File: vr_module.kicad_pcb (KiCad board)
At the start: 4 copper layers, 16.9 x 22.6 mm, 32 parts, among them J1 Conn_01x07, U1 LM393, U2 NC7SB3157P6X, U3 74HC00, U4 NC7SB3157P6X, U5 SRV05-4, U6 MCP6004

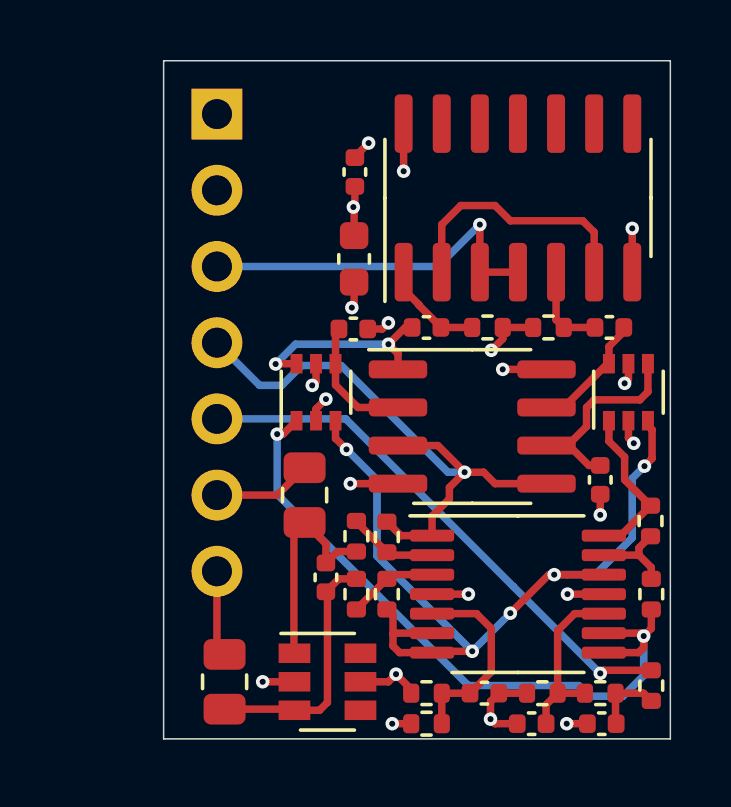
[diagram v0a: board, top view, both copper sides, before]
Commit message: ground unused inputs to NAND
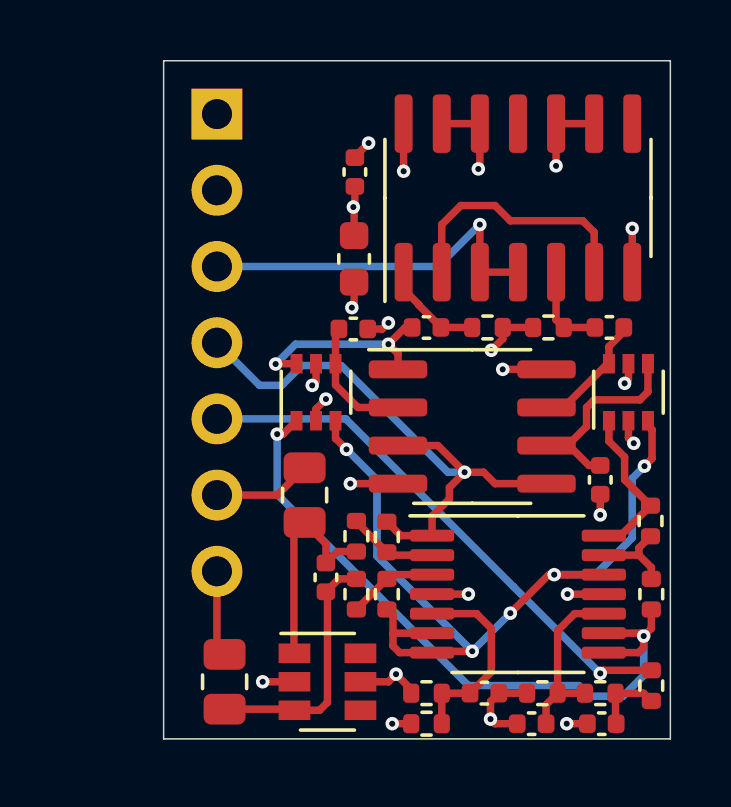
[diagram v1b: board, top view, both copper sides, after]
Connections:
- U3 pad 10: (no net) -> GND
- U3 pad 12: (no net) -> GND
- U3 pad 13: (no net) -> GND
- U3 pad 9: (no net) -> GND
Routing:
- net GND: track 16.1 -> 21.6 mm, vias 14 -> 16

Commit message: upgrade comparator
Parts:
- U1: value LM393 -> MAX9142

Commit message: I heard we like LEDs
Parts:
- added D1: LED, LED_SMD:LED_0603_1608Metric, F.Cu at (62.6, 84.8)
- added R16: 2.2k, Resistor_SMD:R_0402_1005Metric, F.Cu at (62.6, 82.2)
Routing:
- net output: track 12.2 -> 14.9 mm
- net Net-(D1-Pad1): track 0.00 -> 1.30 mm
- net GND: track 21.6 -> 22.3 mm, vias 16 -> 17
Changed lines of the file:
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@@
     (thickness 1.6)
     (drawings 11)
-    (tracks 254)
+    (tracks 261)
     (zones 0)
-    (modules 32)
-    (nets 26)
+    (modules 34)
+    (nets 27)
   )
   (page A4)
@@
   (net 24 "Net-(C9-Pad2)")
   (net 25 "Net-(C10-Pad2)")
+  (net 26 "Net-(D1-Pad1)")
   (net_class Default "This is the default net class."
     (clearance 0.1524)
@@
     (add_net "Net-(C8-Pad1)")
     (add_net "Net-(C9-Pad2)")
+    (add_net "Net-(D1-Pad1)")
     (add_net "Net-(R13-Pad1)")
     (add_net "Net-(R3-Pad1)")
@@
     (add_net thresh_input)
     (add_net thresh_low)
+  )
+  (module Resistor_SMD:R_0402_1005Metric (layer F.Cu)
+    (at 62.5904 82.2452 270)
+    (descr "Resistor SMD 0402 (1005 Metric), square (rectangular) end terminal, IPC_7351 nominal, (Body size source: IPC-SM-782 page 72, https://www.pcb-3d.com/wordpress/wp-content/uploads/ipc-sm-782a_amendment_1_and_2.pdf), generated with kicad-footprint-generator")
+    (tags resistor)
+    (attr smd)
+    (fp_text reference R16 (at 0 -1.17 90) (layer F.SilkS) hide
+      (effects (font (size 1 1) (thickness 0.15)))
+    )
+    (fp_text value 2.2k (at 0 1.17 90) (layer F.Fab)
+      (effects (font (size 1 1) (thickness 0.15)))
+    )
+    (fp_text user %R (at 0 0 90) (layer F.Fab)
+      (effects (font (size 0.26 0.26) (thickness 0.04)))
+    )
+    (fp_line (start -0.525 0.27) (end -0.525 -0.27) (layer F.Fab) (width 0.1))
+    (fp_line (start -0.525 -0.27) (end 0.525 -0.27) (layer F.Fab) (width 0.1))
+    (fp_line (start 0.525 -0.27) (end 0.525 0.27) (layer F.Fab) (width 0.1))
+    (fp_line (start 0.525 0.27) (end -0.525 0.27) (layer F.Fab) (width 0.1))
+    (fp_line (start -0.153641 -0.38) (end 0.153641 -0.38) (layer F.SilkS) (width 0.12))
+    (fp_line (start -0.153641 0.38) (end 0.153641 0.38) (layer F.SilkS) (width 0.12))
+    (fp_line (start -0.93 0.47) (end -0.93 -0.47) (layer F.CrtYd) (width 0.05))
+    (fp_line (start -0.93 -0.47) (end 0.93 -0.47) (layer F.CrtYd) (width 0.05))
+    (fp_line (start 0.93 -0.47) (end 0.93 0.47) (layer F.CrtYd) (width 0.05))
+    (fp_line (start 0.93 0.47) (end -0.93 0.47) (layer F.CrtYd) (width 0.05))
+    (pad 2 smd roundrect (at 0.51 0 270) (size 0.54 0.64) (layers F.Cu F.Paste F.Mask) (roundrect_rratio 0.25)
+      (net 26 "Net-(D1-Pad1)"))
+    (pad 1 smd roundrect (at -0.51 0 270) (size 0.54 0.64) (layers F.Cu F.Paste F.Mask) (roundrect_rratio 0.25)
+      (net 5 GND))
+    (model ${KISYS3DMOD}/Resistor_SMD.3dshapes/R_0402_1005Metric.wrl
+      (at (xyz 0 0 0))
+      (scale (xyz 1 1 1))
+      (rotate (xyz 0 0 0))
+    )
+  )
+  (module LED_SMD:LED_0603_1608Metric (layer F.Cu)
+    (at 62.5856 84.836 270)
+    (descr "LED SMD 0603 (1608 Metric), square (rectangular) end terminal, IPC_7351 nominal, (Body size source: http://www.tortai-tech.com/upload/download/2011102023233369053.pdf), generated with kicad-footprint-generator")
+    (tags LED)
+    (attr smd)
+    (fp_text reference D1 (at 0 -1.43 90) (layer F.SilkS) hide
+      (effects (font (size 1 1) (thickness 0.15)))
+    )
+    (fp_text value LED (at 0 1.43 90) (layer F.Fab)
+      (effects (font (size 1 1) (thickness 0.15)))
+    )
+    (fp_text user %R (at 0 0 90) (layer F.Fab)
+      (effects (font (size 0.4 0.4) (thickness 0.06)))
+    )
+    (fp_line (start 0.8 -0.4) (end -0.5 -0.4) (layer F.Fab) (width 0.1))
+    (fp_line (start -0.5 -0.4) (end -0.8 -0.1) (layer F.Fab) (width 0.1))
+    (fp_line (start -0.8 -0.1) (end -0.8 0.4) (layer F.Fab) (width 0.1))
+    (fp_line (start -0.8 0.4) (end 0.8 0.4) (layer F.Fab) (width 0.1))
+    (fp_line (start 0.8 0.4) (end 0.8 -0.4) (layer F.Fab) (width 0.1))
+    (fp_line (start 0.8 -0.735) (end -1.485 -0.735) (layer F.SilkS) (width 0.12))
+    (fp_line (start -1.485 -0.735) (end -1.485 0.735) (layer F.SilkS) (width 0.12))
+    (fp_line (start -1.485 0.735) (end 0.8 0.735) (layer F.SilkS) (width 0.12))
+    (fp_line (start -1.48 0.73) (end -1.48 -0.73) (layer F.CrtYd) (width 0.05))
+    (fp_line (start -1.48 -0.73) (end 1.48 -0.73) (layer F.CrtYd) (width 0.05))
+    (fp_line (start 1.48 -0.73) (end 1.48 0.73) (layer F.CrtYd) (width 0.05))
+    (fp_line (start 1.48 0.73) (end -1.48 0.73) (layer F.CrtYd) (width 0.05))
+    (pad 2 smd roundrect (at 0.7875 0 270) (size 0.875 0.95) (layers F.Cu F.Paste F.Mask) (roundrect_rratio 0.25)
+      (net 21 output))
+    (pad 1 smd roundrect (at -0.7875 0 270) (size 0.875 0.95) (layers F.Cu F.Paste F.Mask) (roundrect_rratio 0.25)
+      (net 26 "Net-(D1-Pad1)"))
+    (model ${KISYS3DMOD}/LED_SMD.3dshapes/LED_0603_1608Metric.wrl
+      (at (xyz 0 0 0))
+      (scale (xyz 1 1 1))
+      (rotate (xyz 0 0 0))
+    )
   )
   (module Capacitor_SMD:C_0402_1005Metric (layer F.Cu)
@@
   (via (at 71.374 81.7372) (size 0.45) (drill 0.2) (layers F.Cu B.Cu) (net 5))
   (segment (start 71.374 80.329) (end 71.374 81.7372) (width 0.25) (layer F.Cu) (net 5))
+  (segment (start 62.5904 81.0308) (end 62.5856 81.026) (width 0.25) (layer F.Cu) (net 5))
+  (via (at 62.5856 81.026) (size 0.45) (drill 0.2) (layers F.Cu B.Cu) (net 5))
+  (segment (start 62.5904 81.7352) (end 62.5904 81.0308) (width 0.25) (layer F.Cu) (net 5))
   (via (at 68.453 96.012) (size 0.45) (drill 0.2) (layers F.Cu B.Cu) (net 6))
   (segment (start 67.2415 96.012) (end 68.453 96.012) (width 0.25) (layer F.Cu) (net 6))
@@
   (segment (start 67.437 85.09) (end 60.071 85.09) (width 0.25) (layer B.Cu) (net 21))
   (segment (start 68.834 83.693) (end 67.437 85.09) (width 0.25) (layer B.Cu) (net 21))
+  (segment (start 62.0521 85.09) (end 60.071 85.09) (width 0.25) (layer F.Cu) (net 21))
+  (segment (start 62.5856 85.6235) (end 62.0521 85.09) (width 0.25) (layer F.Cu) (net 21))
   (via (at 68.326 91.948) (size 0.45) (drill 0.2) (layers F.Cu B.Cu) (net 22))
   (segment (start 67.437 91.059) (end 68.326 91.948) (width 0.25) (layer F.Cu) (net 22))
@@
   (segment (start 71.8058 91.059) (end 71.055 91.059) (width 0.25) (layer F.Cu) (net 25))
   (segment (start 72.4688 91.722) (end 71.8058 91.059) (width 0.25) (layer F.Cu) (net 25))
+  (segment (start 62.5856 82.76) (end 62.5904 82.7552) (width 0.25) (layer F.Cu) (net 26))
+  (segment (start 62.5856 84.0485) (end 62.5856 82.76) (width 0.25) (layer F.Cu) (net 26))
   (zone (net 5) (net_name GND) (layer In1.Cu) (hatch edge 0.508)
     (connect_pads (clearance 0.254))

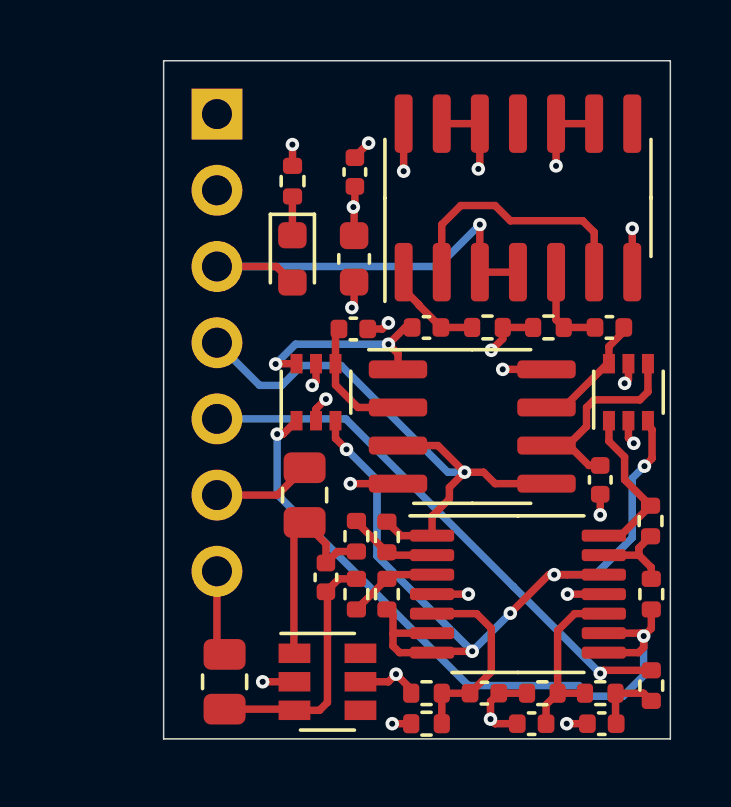
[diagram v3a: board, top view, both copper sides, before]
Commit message: oh no one comparator was flipped
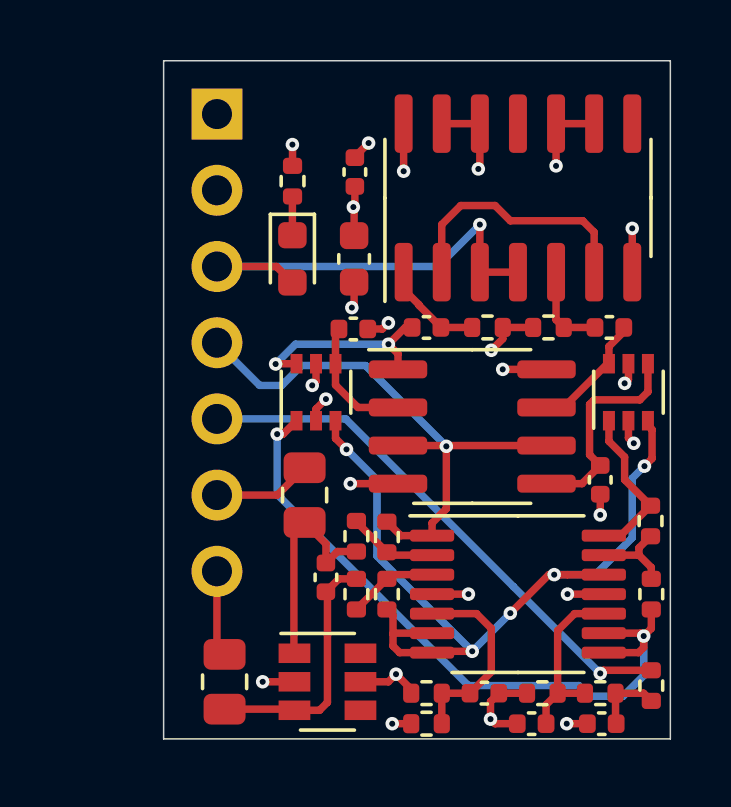
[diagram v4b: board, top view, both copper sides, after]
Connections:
- U1 pad 5: analog_out -> Net-(C10-Pad2)
- U1 pad 6: Net-(C10-Pad2) -> analog_out
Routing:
- net analog_out: track 20.3 -> 20.9 mm
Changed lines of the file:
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@@
     (thickness 1.6)
     (drawings 11)
-    (tracks 261)
+    (tracks 258)
     (zones 0)
     (modules 34)
@@
       (net 3 "Net-(C2-Pad2)"))
     (pad 6 smd roundrect (at 2.475 0.635) (size 1.95 0.6) (layers F.Cu F.Paste F.Mask) (roundrect_rratio 0.25)
+      (net 22 analog_out))
+    (pad 5 smd roundrect (at 2.475 1.905) (size 1.95 0.6) (layers F.Cu F.Paste F.Mask) (roundrect_rratio 0.25)
       (net 25 "Net-(C10-Pad2)"))
-    (pad 5 smd roundrect (at 2.475 1.905) (size 1.95 0.6) (layers F.Cu F.Paste F.Mask) (roundrect_rratio 0.25)
-      (net 22 analog_out))
     (pad 4 smd roundrect (at -2.475 1.905) (size 1.95 0.6) (layers F.Cu F.Paste F.Mask) (roundrect_rratio 0.25)
       (net 5 GND))
@@
   (segment (start 62.0521 85.09) (end 60.071 85.09) (width 0.25) (layer F.Cu) (net 21))
   (segment (start 62.5856 85.6235) (end 62.0521 85.09) (width 0.25) (layer F.Cu) (net 21))
-  (via (at 68.326 91.948) (size 0.45) (drill 0.2) (layers F.Cu B.Cu) (net 22))
-  (segment (start 67.437 91.059) (end 68.326 91.948) (width 0.25) (layer F.Cu) (net 22))
-  (segment (start 66.105 91.059) (end 67.437 91.059) (width 0.25) (layer F.Cu) (net 22))
-  (segment (start 67.2415 94.062) (end 67.2415 93.4135) (width 0.25) (layer F.Cu) (net 22))
-  (segment (start 67.2415 93.4135) (end 67.818 92.837) (width 0.25) (layer F.Cu) (net 22))
-  (segment (start 67.818 92.456) (end 68.326 91.948) (width 0.25) (layer F.Cu) (net 22))
-  (segment (start 67.818 92.837) (end 67.818 92.456) (width 0.25) (layer F.Cu) (net 22))
-  (segment (start 68.326 91.948) (end 68.961 91.948) (width 0.25) (layer F.Cu) (net 22))
-  (segment (start 69.342 92.329) (end 71.055 92.329) (width 0.25) (layer F.Cu) (net 22))
-  (segment (start 68.961 91.948) (end 69.342 92.329) (width 0.25) (layer F.Cu) (net 22))
   (segment (start 66.2002 94.062) (end 65.7352 93.597) (width 0.25) (layer F.Cu) (net 22))
   (segment (start 67.2415 94.062) (end 66.2002 94.062) (width 0.25) (layer F.Cu) (net 22))
-  (segment (start 60.071 87.63) (end 61.4934 89.0524) (width 0.25) (layer B.Cu) (net 22))
-  (segment (start 61.4934 89.0524) (end 62.23 89.0524) (width 0.25) (layer B.Cu) (net 22))
-  (segment (start 62.23 89.0524) (end 62.8904 88.392) (width 0.25) (layer B.Cu) (net 22))
-  (segment (start 62.8904 88.392) (end 64.2112 88.392) (width 0.25) (layer B.Cu) (net 22))
-  (segment (start 67.7672 91.948) (end 68.326 91.948) (width 0.25) (layer B.Cu) (net 22))
-  (segment (start 64.2112 88.392) (end 67.7672 91.948) (width 0.25) (layer B.Cu) (net 22))
   (segment (start 74.293 99.314) (end 74.549 99.57) (width 0.25) (layer F.Cu) (net 23))
   (segment (start 73.3572 99.314) (end 74.293 99.314) (width 0.25) (layer F.Cu) (net 23))
@@
   (segment (start 64.023 87.2874) (end 64.1376 87.1728) (width 0.25) (layer F.Cu) (net 24))
   (segment (start 64.023 88.331) (end 64.023 87.2874) (width 0.25) (layer F.Cu) (net 24))
-  (segment (start 71.055 91.059) (end 71.755 91.059) (width 0.25) (layer F.Cu) (net 25))
-  (segment (start 72.39 90.424) (end 72.39 89.789) (width 0.25) (layer F.Cu) (net 25))
-  (segment (start 71.755 91.059) (end 72.39 90.424) (width 0.25) (layer F.Cu) (net 25))
-  (segment (start 72.39 89.789) (end 72.644 89.535) (width 0.25) (layer F.Cu) (net 25))
+  (segment (start 71.055 91.059) (end 71.755 91.059) (width 0.25) (layer F.Cu) (net 22))
   (segment (start 72.644 89.535) (end 74.168 89.535) (width 0.25) (layer F.Cu) (net 25))
   (segment (start 74.437 89.266) (end 74.437 88.331) (width 0.25) (layer F.Cu) (net 25))
   (segment (start 74.168 89.535) (end 74.437 89.266) (width 0.25) (layer F.Cu) (net 25))
-  (segment (start 72.8472 91.722) (end 72.4688 91.722) (width 0.25) (layer F.Cu) (net 25))
-  (segment (start 71.8058 91.059) (end 71.055 91.059) (width 0.25) (layer F.Cu) (net 25))
-  (segment (start 72.4688 91.722) (end 71.8058 91.059) (width 0.25) (layer F.Cu) (net 25))
+  (segment (start 71.8058 91.059) (end 71.055 91.059) (width 0.25) (layer F.Cu) (net 22))
+  (via (at 67.7164 91.0844) (size 0.45) (drill 0.2) (layers F.Cu B.Cu) (net 22))
+  (segment (start 67.691 91.059) (end 67.7164 91.0844) (width 0.25) (layer F.Cu) (net 22))
+  (segment (start 66.105 91.059) (end 67.691 91.059) (width 0.25) (layer F.Cu) (net 22))
+  (segment (start 67.7418 91.059) (end 67.7164 91.0844) (width 0.25) (layer F.Cu) (net 22))
+  (segment (start 71.055 91.059) (end 67.7418 91.059) (width 0.25) (layer F.Cu) (net 22))
+  (segment (start 65.024 88.392) (end 67.7164 91.0844) (width 0.25) (layer B.Cu) (net 22))
+  (segment (start 62.23 89.0524) (end 62.8904 88.392) (width 0.25) (layer B.Cu) (net 22))
+  (segment (start 62.8904 88.392) (end 65.024 88.392) (width 0.25) (layer B.Cu) (net 22))
+  (segment (start 61.4934 89.0524) (end 62.23 89.0524) (width 0.25) (layer B.Cu) (net 22))
+  (segment (start 60.071 87.63) (end 61.4934 89.0524) (width 0.25) (layer B.Cu) (net 22))
+  (segment (start 67.2415 94.062) (end 67.2415 93.6421) (width 0.25) (layer F.Cu) (net 22))
+  (segment (start 67.7164 93.1672) (end 67.7164 91.0844) (width 0.25) (layer F.Cu) (net 22))
+  (segment (start 67.2415 93.6421) (end 67.7164 93.1672) (width 0.25) (layer F.Cu) (net 22))
+  (segment (start 72.644 89.535) (end 72.4916 89.6874) (width 0.25) (layer F.Cu) (net 25))
+  (segment (start 72.4916 91.3664) (end 72.8472 91.722) (width 0.25) (layer F.Cu) (net 25))
+  (segment (start 72.4916 89.6874) (end 72.4916 91.3664) (width 0.25) (layer F.Cu) (net 25))
+  (segment (start 72.2402 92.329) (end 72.8472 91.722) (width 0.25) (layer F.Cu) (net 25))
+  (segment (start 71.055 92.329) (end 72.2402 92.329) (width 0.25) (layer F.Cu) (net 25))
   (segment (start 62.5856 82.76) (end 62.5904 82.7552) (width 0.25) (layer F.Cu) (net 26))
   (segment (start 62.5856 84.0485) (end 62.5856 82.76) (width 0.25) (layer F.Cu) (net 26))

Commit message: export
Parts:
- moved J1 3.43 mm to (56.6, 80.0)
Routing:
- net output: track 14.9 -> 21.8 mm
- net thresh_input: track 18.0 -> 21.5 mm
- net analog_out: track 20.9 -> 24.3 mm
- net VR-: track 3.30 -> 6.73 mm
- net VR+: track 2.88 -> 5.80 mm
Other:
- board size 16.9 x 22.6 mm -> 20.3 x 22.9 mm
- board text added: "Analog"
- board text added: "Out"
- board text added: "Thresh"
- board text removed: "Analog out"
- board text removed: "Output"
- board text removed: "Threshold input"

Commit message: rev b improvements
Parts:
- added C11: 1u, Capacitor_SMD:C_0402_1005Metric, F.Cu at (74.2, 91.0)
- added C12: 1u, Capacitor_SMD:C_0402_1005Metric, F.Cu at (72.3, 91.0)
- added C13: 100n, Capacitor_SMD:C_0402_1005Metric, F.Cu at (67.5, 99.9)
- added C14: 10n, Capacitor_SMD:C_0402_1005Metric, F.Cu at (70.2, 88.2)
- added C15: 1u, Capacitor_SMD:C_0402_1005Metric, F.Cu at (71.1, 88.2)
- added C16: 10n, Capacitor_SMD:C_0402_1005Metric, F.Cu at (65.4, 95.9)
- added C17: 1u, Capacitor_SMD:C_0402_1005Metric, F.Cu at (64.4, 95.9)
- added R17: 10, Resistor_SMD:R_0402_1005Metric, F.Cu at (60.2, 94.0)
- added R18: 10, Resistor_SMD:R_0402_1005Metric, F.Cu at (65.3, 93.3)
- added R19: 10, Resistor_SMD:R_0402_1005Metric, F.Cu at (72.8, 92.6)
- C10, C9: value 10n -> 1u
- C7: footprint Capacitor_SMD:C_0603_1608Metric -> Capacitor_SMD:C_0402_1005Metric
- U3: value 74HC00 -> 74HC02
- moved C10 11.1 mm to (61.7, 92.5), turned to 270 degrees
- moved C9 6.97 mm to (60.1, 92.5), turned to 270 degrees
- moved R7 6.67 mm to (58.7, 97.8)
- moved R9 6.51 mm to (63.0, 94.2)
- moved C4 6.26 mm to (65.3, 94.2), turned to 180 degrees
- moved R10 6.19 mm to (63.0, 95.7), turned to 270 degrees
- moved R16 5.39 mm to (59.8, 86.9)
- moved C7 5.08 mm to (62.0, 80.5)
- moved C5 4.38 mm to (64.3, 99.8)
- moved R5 4.35 mm to (66.0, 100.4), turned to 0 degrees
- moved R3 3.81 mm to (64.7, 97.9)
- moved R6 3.78 mm to (65.7, 97.9), turned to 90 degrees
- moved R8 3.69 mm to (56.6, 99.1)
- moved R4 3.50 mm to (65.7, 99.4), turned to 0 degrees
- moved U1 2.69 mm to (65.9, 90.0)
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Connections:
- C10 pad 1: GND -> Vref
- C10 pad 2: Net-(C10-Pad2) -> GND
- C9 pad 1: GND -> thresh_low
- C9 pad 2: Net-(C9-Pad2) -> GND
- R11 pad 1: Net-(C8-Pad1) -> Net-(C3-Pad1)
- R11 pad 2: Net-(C3-Pad1) -> Net-(C8-Pad1)
- R13 pad 2: thresh_low -> Net-(R13-Pad2)
- R14 pad 1: thresh_high -> Net-(R14-Pad1)
- U1 pad 2: Net-(C9-Pad2) -> Net-(U1-Pad2)
- U1 pad 5: Net-(C10-Pad2) -> Net-(U1-Pad5)
- U2 pad 4: Net-(C9-Pad2) -> Net-(U1-Pad2)
- U3 pad 1: Net-(C1-Pad1) -> output
- U3 pad 10: GND -> (no net)
- U3 pad 11: (no net) -> GND
- U3 pad 13: GND -> (no net)
- U3 pad 2: Net-(U3-Pad2) -> Net-(C1-Pad1)
- U3 pad 3: output -> Net-(U3-Pad3)
- U3 pad 4: output -> Net-(U3-Pad3)
- U3 pad 5: Net-(C2-Pad1) -> output
- U3 pad 6: Net-(U3-Pad2) -> Net-(C2-Pad1)
- U3 pad 8: (no net) -> GND
- U4 pad 4: Net-(C10-Pad2) -> Net-(U1-Pad5)
- U5 pad 4: (no net) -> Net-(C5-Pad2)
- U5 pad 6: (no net) -> Net-(C5-Pad1)
- U6 pad 1: analog_out -> Net-(R18-Pad1)
- U6 pad 14: thresh_high -> Net-(R14-Pad1)
- U6 pad 2: Net-(R3-Pad1) -> Net-(R18-Pad1)
- U6 pad 3: Net-(R4-Pad2) -> Net-(C4-Pad1)
- U6 pad 5: Net-(C4-Pad1) -> Net-(R4-Pad2)
- U6 pad 6: Vref -> Net-(R3-Pad1)
- U6 pad 7: Vref -> analog_out
- U6 pad 8: thresh_low -> Net-(R13-Pad2)
- U6 pad 9: thresh_low -> Net-(R13-Pad2)
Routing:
- net Net-(R13-Pad2): track 0.00 -> 20.0 mm, vias 0 -> 2
- net thresh_low: track 23.6 -> 3.63 mm, vias 2 -> 0
- net Net-(U3-Pad2): track 8.63 -> 0.00 mm
- net Net-(U1-Pad5): track 0.00 -> 8.47 mm
- net Net-(C10-Pad2): track 7.28 -> 0.00 mm
- net Net-(R18-Pad1): track 0.00 -> 4.61 mm
- net Net-(C9-Pad2): track 4.31 -> 0.00 mm
- net GND: track 22.3 -> 26.5 mm, vias 17 -> 23
- net +5V: track 9.55 -> 13.5 mm
- net analog_out: track 24.3 -> 28.2 mm
- net Net-(C2-Pad2): track 4.10 -> 7.86 mm
- net output: track 21.8 -> 18.0 mm, vias 1 -> 0
- net Net-(R14-Pad1): track 0.00 -> 3.41 mm
- net Net-(R4-Pad2): track 3.01 -> 6.02 mm, vias 0 -> 2
- net VR+: track 5.80 -> 2.90 mm
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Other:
- board text added: "A"
- board text added: "T"
- board text added: "V+"
- board text added: "V-"
- board text added: "rev B"
- board text removed: "Analog"
- board text removed: "Thresh"
- board text removed: "VR+"
- board text removed: "VR-"
